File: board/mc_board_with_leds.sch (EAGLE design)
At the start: 30 parts, among them IC2 MEGA8-P, Q2 16MHz

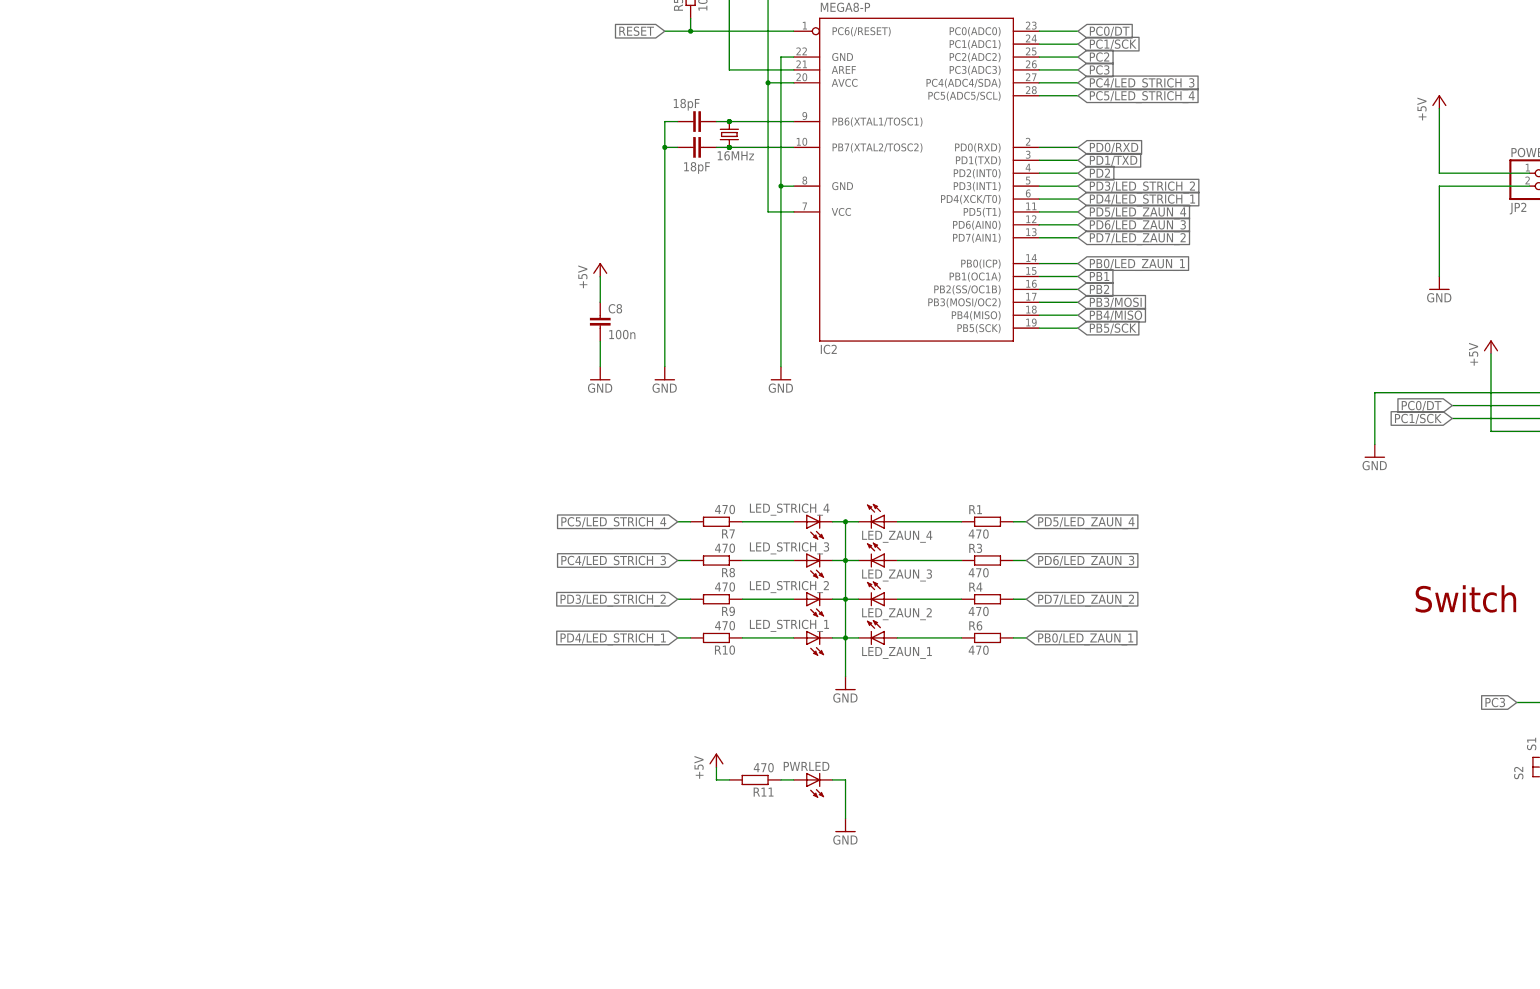
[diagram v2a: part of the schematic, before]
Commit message: added step up converter to schematic
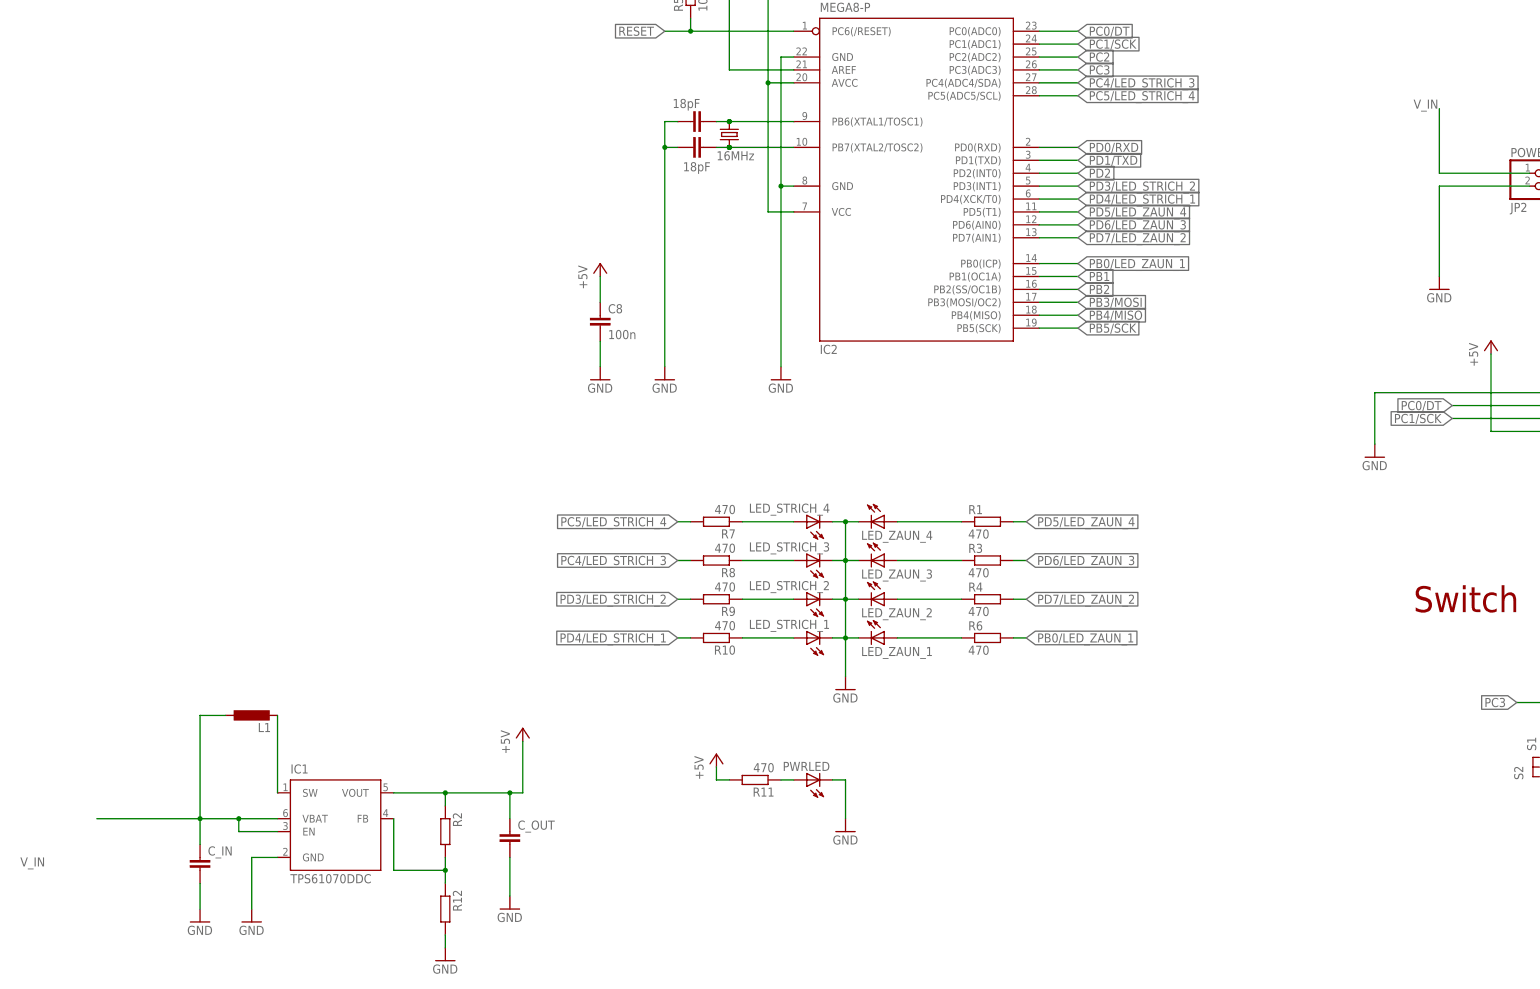
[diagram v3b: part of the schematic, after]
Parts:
- added C_IN, C_OUT: (no value), rcl-2:C-EUC0805
- added IC1: TPS61070DDC, texas:TPS61070DDC
- added L1: (no value), rcl:L-EUL4532P
- added R12, R2: (no value), resistor:R-EU_R0805
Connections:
- new net N$5: IC1.SW, L1.2
- new net N$6: IC1.FB, R12.1, R2.2
- new net V_IN: C_IN.1, IC1.EN, IC1.VBAT, L1.1, POWER1.1
- net +5V: now also C_OUT.1, IC1.VOUT, R2.1; no longer POWER1.1
- net GND: now also C_IN.2, C_OUT.2, IC1.GND, R12.2
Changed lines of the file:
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@@
 <part name="GND16" library="supply1" deviceset="GND" device=""/>
 <part name="POWER1" library="pinhead" deviceset="PINHD-1X2" device="" value="JP2"/>
-<part name="P+16" library="supply1" deviceset="+5V" device=""/>
 <part name="GND17" library="supply1" deviceset="GND" device=""/>
 <part name="HX1" library="pinhead" deviceset="PINHD-1X4" device="" value="JP1"/>
@@
 <part name="P+17" library="supply1" deviceset="+5V" device=""/>
 <part name="UART1" library="pinhead" deviceset="PINHD-1X2" device="" value="JP2"/>
+<part name="IC1" library="texas" deviceset="TPS6107*" device="DDC" technology="0"/>
+<part name="L1" library="rcl" deviceset="L-EU" device="L4532P"/>
+<part name="R2" library="resistor" deviceset="R-EU_" device="R0805"/>
+<part name="R12" library="resistor" deviceset="R-EU_" device="R0805"/>
+<part name="C_IN" library="rcl-2" deviceset="C-EU" device="C0805"/>
+<part name="C_OUT" library="rcl-2" deviceset="C-EU" device="C0805"/>
+<part name="GND1" library="supply1" deviceset="GND" device=""/>
+<part name="GND2" library="supply1" deviceset="GND" device=""/>
+<part name="P+1" library="supply1" deviceset="+5V" device=""/>
+<part name="GND3" library="supply1" deviceset="GND" device=""/>
+<part name="GND4" library="supply1" deviceset="GND" device=""/>
 </parts>
 <sheets>
@@
 <instance part="GND16" gate="1" x="327.66" y="109.22"/>
 <instance part="POWER1" gate="G$1" x="314.96" y="78.74"/>
-<instance part="P+16" gate="1" x="294.64" y="96.52"/>
 <instance part="GND17" gate="1" x="294.64" y="58.42"/>
 <instance part="HX1" gate="A" x="325.12" y="33.02"/>
@@
 <instance part="P+17" gate="1" x="304.8" y="48.26"/>
 <instance part="UART1" gate="G$1" x="353.06" y="60.96"/>
+<instance part="IC1" gate="G$1" x="76.2" y="-48.26"/>
+<instance part="L1" gate="G$1" x="60.96" y="-25.4" rot="R90"/>
+<instance part="R2" gate="G$1" x="99.06" y="-48.26" rot="R270"/>
+<instance part="R12" gate="G$1" x="99.06" y="-63.5" rot="R270"/>
+<instance part="C_IN" gate="G$1" x="50.8" y="-53.34"/>
+<instance part="C_OUT" gate="G$1" x="111.76" y="-48.26"/>
+<instance part="GND1" gate="1" x="50.8" y="-66.04"/>
+<instance part="GND2" gate="1" x="60.96" y="-66.04"/>
+<instance part="P+1" gate="1" x="114.3" y="-27.94"/>
+<instance part="GND3" gate="1" x="99.06" y="-73.66"/>
+<instance part="GND4" gate="1" x="111.76" y="-63.5"/>
 </instances>
 <busses>
@@
 <wire x1="281.94" y1="38.1" x2="281.94" y2="27.94" width="0.1524" layer="91"/>
 </segment>
+<segment>
+<pinref part="C_IN" gate="G$1" pin="2"/>
+<pinref part="GND1" gate="1" pin="GND"/>
+<wire x1="50.8" y1="-58.42" x2="50.8" y2="-63.5" width="0.1524" layer="91"/>
+</segment>
+<segment>
+<pinref part="GND2" gate="1" pin="GND"/>
+<pinref part="IC1" gate="G$1" pin="GND"/>
+<wire x1="60.96" y1="-63.5" x2="60.96" y2="-53.34" width="0.1524" layer="91"/>
+<wire x1="60.96" y1="-53.34" x2="66.04" y2="-53.34" width="0.1524" layer="91"/>
+</segment>
+<segment>
+<pinref part="GND4" gate="1" pin="GND"/>
+<pinref part="C_OUT" gate="G$1" pin="2"/>
+<wire x1="111.76" y1="-60.96" x2="111.76" y2="-53.34" width="0.1524" layer="91"/>
+</segment>
+<segment>
+<pinref part="GND3" gate="1" pin="GND"/>
+<pinref part="R12" gate="G$1" pin="2"/>
+<wire x1="99.06" y1="-71.12" x2="99.06" y2="-68.58" width="0.1524" layer="91"/>
+</segment>
 </net>
 <net name="N$8" class="0">
@@
 </segment>
 <segment>
-<pinref part="P+16" gate="1" pin="+5V"/>
-<wire x1="294.64" y1="93.98" x2="294.64" y2="81.28" width="0.1524" layer="91"/>
-<pinref part="POWER1" gate="G$1" pin="1"/>
-<wire x1="294.64" y1="81.28" x2="312.42" y2="81.28" width="0.1524" layer="91"/>
-</segment>
-<segment>
 <pinref part="HX1" gate="A" pin="4"/>
 <wire x1="322.58" y1="30.48" x2="304.8" y2="30.48" width="0.1524" layer="91"/>
 <pinref part="P+17" gate="1" pin="+5V"/>
 <wire x1="304.8" y1="30.48" x2="304.8" y2="45.72" width="0.1524" layer="91"/>
+</segment>
+<segment>
+<pinref part="IC1" gate="G$1" pin="VOUT"/>
+<wire x1="88.9" y1="-40.64" x2="99.06" y2="-40.64" width="0.1524" layer="91"/>
+<pinref part="R2" gate="G$1" pin="1"/>
+<wire x1="99.06" y1="-40.64" x2="111.76" y2="-40.64" width="0.1524" layer="91"/>
+<wire x1="111.76" y1="-40.64" x2="114.3" y2="-40.64" width="0.1524" layer="91"/>
+<wire x1="99.06" y1="-43.18" x2="99.06" y2="-40.64" width="0.1524" layer="91"/>
+<junction x="99.06" y="-40.64"/>
+<pinref part="P+1" gate="1" pin="+5V"/>
+<wire x1="114.3" y1="-40.64" x2="114.3" y2="-30.48" width="0.1524" layer="91"/>
+<pinref part="C_OUT" gate="G$1" pin="1"/>
+<wire x1="111.76" y1="-45.72" x2="111.76" y2="-40.64" width="0.1524" layer="91"/>
+<junction x="111.76" y="-40.64"/>
 </segment>
 </net>
@@
 </segment>
 </net>
+<net name="V_IN" class="0">
+<segment>
+<wire x1="294.64" y1="93.98" x2="294.64" y2="81.28" width="0.1524" layer="91"/>
+<pinref part="POWER1" gate="G$1" pin="1"/>
+<wire x1="294.64" y1="81.28" x2="312.42" y2="81.28" width="0.1524" layer="91"/>
+<label x="289.56" y="93.98" size="1.778" layer="95"/>
+</segment>
+<segment>
+<pinref part="IC1" gate="G$1" pin="VBAT"/>
+<wire x1="66.04" y1="-45.72" x2="58.42" y2="-45.72" width="0.1524" layer="91"/>
+<pinref part="C_IN" gate="G$1" pin="1"/>
+<wire x1="58.42" y1="-45.72" x2="50.8" y2="-45.72" width="0.1524" layer="91"/>
+<wire x1="50.8" y1="-45.72" x2="30.48" y2="-45.72" width="0.1524" layer="91"/>
+<wire x1="50.8" y1="-50.8" x2="50.8" y2="-45.72" width="0.1524" layer="91"/>
+<junction x="50.8" y="-45.72"/>
+<label x="20.32" y="-53.34" size="1.778" layer="95" rot="R180"/>
+<pinref part="L1" gate="G$1" pin="1"/>
+<wire x1="55.88" y1="-25.4" x2="50.8" y2="-25.4" width="0.1524" layer="91"/>
+<wire x1="50.8" y1="-25.4" x2="50.8" y2="-45.72" width="0.1524" layer="91"/>
+<pinref part="IC1" gate="G$1" pin="EN"/>
+<wire x1="66.04" y1="-48.26" x2="58.42" y2="-48.26" width="0.1524" layer="91"/>
+<wire x1="58.42" y1="-48.26" x2="58.42" y2="-45.72" width="0.1524" layer="91"/>
+<junction x="58.42" y="-45.72"/>
+</segment>
+</net>
+<net name="N$5" class="0">
+<segment>
+<pinref part="IC1" gate="G$1" pin="SW"/>
+<pinref part="L1" gate="G$1" pin="2"/>
+<wire x1="66.04" y1="-40.64" x2="66.04" y2="-25.4" width="0.1524" layer="91"/>
+</segment>
+</net>
+<net name="N$6" class="0">
+<segment>
+<pinref part="R12" gate="G$1" pin="1"/>
+<pinref part="R2" gate="G$1" pin="2"/>
+<wire x1="99.06" y1="-58.42" x2="99.06" y2="-55.88" width="0.1524" layer="91"/>
+<pinref part="IC1" gate="G$1" pin="FB"/>
+<wire x1="99.06" y1="-55.88" x2="99.06" y2="-53.34" width="0.1524" layer="91"/>
+<wire x1="88.9" y1="-45.72" x2="88.9" y2="-55.88" width="0.1524" layer="91"/>
+<wire x1="88.9" y1="-55.88" x2="99.06" y2="-55.88" width="0.1524" layer="91"/>
+<junction x="99.06" y="-55.88"/>
+</segment>
+</net>

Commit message: added missing values
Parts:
- C_IN: value (none) -> 4.7μF
- C_OUT: value (none) -> 47μF
- L1: value (none) -> 4,7µH
- R_BOT: value (none) -> 330k
- R_TOP: value (none) -> 560k
- renumbered IC1 to MCP1640BT-I, R12 to R_BOT, R2 to R_TOP
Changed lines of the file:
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@@
 <part name="P+17" library="supply1" deviceset="+5V" device=""/>
 <part name="UART1" library="pinhead" deviceset="PINHD-1X2" device="" value="JP2"/>
-<part name="IC1" library="texas" deviceset="TPS6107*" device="DDC" technology="0"/>
-<part name="L1" library="rcl" deviceset="L-EU" device="L4532P"/>
-<part name="R2" library="resistor" deviceset="R-EU_" device="R0805"/>
-<part name="R12" library="resistor" deviceset="R-EU_" device="R0805"/>
-<part name="C_IN" library="rcl-2" deviceset="C-EU" device="C0805"/>
-<part name="C_OUT" library="rcl-2" deviceset="C-EU" device="C0805"/>
+<part name="MCP1640BT-I" library="texas" deviceset="TPS6107*" device="DDC" technology="0"/>
+<part name="L1" library="rcl" deviceset="L-EU" device="L4532P" value="4,7µH"/>
+<part name="R_TOP" library="resistor" deviceset="R-EU_" device="R0805" value="560k"/>
+<part name="R_BOT" library="resistor" deviceset="R-EU_" device="R0805" value="330k"/>
+<part name="C_IN" library="rcl-2" deviceset="C-EU" device="C0805" value="4.7μF"/>
+<part name="C_OUT" library="rcl-2" deviceset="C-EU" device="C0805" value="47μF"/>
 <part name="GND1" library="supply1" deviceset="GND" device=""/>
 <part name="GND2" library="supply1" deviceset="GND" device=""/>
@@
 <instance part="P+17" gate="1" x="304.8" y="48.26"/>
 <instance part="UART1" gate="G$1" x="353.06" y="60.96"/>
-<instance part="IC1" gate="G$1" x="76.2" y="-48.26"/>
+<instance part="MCP1640BT-I" gate="G$1" x="76.2" y="-48.26"/>
 <instance part="L1" gate="G$1" x="60.96" y="-25.4" rot="R90"/>
-<instance part="R2" gate="G$1" x="99.06" y="-48.26" rot="R270"/>
-<instance part="R12" gate="G$1" x="99.06" y="-63.5" rot="R270"/>
+<instance part="R_TOP" gate="G$1" x="99.06" y="-48.26" rot="R270"/>
+<instance part="R_BOT" gate="G$1" x="99.06" y="-63.5" rot="R270"/>
 <instance part="C_IN" gate="G$1" x="50.8" y="-53.34"/>
 <instance part="C_OUT" gate="G$1" x="111.76" y="-48.26"/>
@@
 <segment>
 <pinref part="GND2" gate="1" pin="GND"/>
-<pinref part="IC1" gate="G$1" pin="GND"/>
+<pinref part="MCP1640BT-I" gate="G$1" pin="GND"/>
 <wire x1="60.96" y1="-63.5" x2="60.96" y2="-53.34" width="0.1524" layer="91"/>
 <wire x1="60.96" y1="-53.34" x2="66.04" y2="-53.34" width="0.1524" layer="91"/>
@@
 <segment>
 <pinref part="GND3" gate="1" pin="GND"/>
-<pinref part="R12" gate="G$1" pin="2"/>
+<pinref part="R_BOT" gate="G$1" pin="2"/>
 <wire x1="99.06" y1="-71.12" x2="99.06" y2="-68.58" width="0.1524" layer="91"/>
 </segment>
@@
 </segment>
 <segment>
-<pinref part="IC1" gate="G$1" pin="VOUT"/>
+<pinref part="MCP1640BT-I" gate="G$1" pin="VOUT"/>
 <wire x1="88.9" y1="-40.64" x2="99.06" y2="-40.64" width="0.1524" layer="91"/>
-<pinref part="R2" gate="G$1" pin="1"/>
+<pinref part="R_TOP" gate="G$1" pin="1"/>
 <wire x1="99.06" y1="-40.64" x2="111.76" y2="-40.64" width="0.1524" layer="91"/>
 <wire x1="111.76" y1="-40.64" x2="114.3" y2="-40.64" width="0.1524" layer="91"/>
@@
 </segment>
 <segment>
-<pinref part="IC1" gate="G$1" pin="VBAT"/>
+<pinref part="MCP1640BT-I" gate="G$1" pin="VBAT"/>
 <wire x1="66.04" y1="-45.72" x2="58.42" y2="-45.72" width="0.1524" layer="91"/>
 <pinref part="C_IN" gate="G$1" pin="1"/>
@@
 <wire x1="55.88" y1="-25.4" x2="50.8" y2="-25.4" width="0.1524" layer="91"/>
 <wire x1="50.8" y1="-25.4" x2="50.8" y2="-45.72" width="0.1524" layer="91"/>
-<pinref part="IC1" gate="G$1" pin="EN"/>
+<pinref part="MCP1640BT-I" gate="G$1" pin="EN"/>
 <wire x1="66.04" y1="-48.26" x2="58.42" y2="-48.26" width="0.1524" layer="91"/>
 <wire x1="58.42" y1="-48.26" x2="58.42" y2="-45.72" width="0.1524" layer="91"/>
@@
 <net name="N$5" class="0">
 <segment>
-<pinref part="IC1" gate="G$1" pin="SW"/>
+<pinref part="MCP1640BT-I" gate="G$1" pin="SW"/>
 <pinref part="L1" gate="G$1" pin="2"/>
 <wire x1="66.04" y1="-40.64" x2="66.04" y2="-25.4" width="0.1524" layer="91"/>
@@
 <net name="N$6" class="0">
 <segment>
-<pinref part="R12" gate="G$1" pin="1"/>
-<pinref part="R2" gate="G$1" pin="2"/>
+<pinref part="R_BOT" gate="G$1" pin="1"/>
+<pinref part="R_TOP" gate="G$1" pin="2"/>
 <wire x1="99.06" y1="-58.42" x2="99.06" y2="-55.88" width="0.1524" layer="91"/>
-<pinref part="IC1" gate="G$1" pin="FB"/>
+<pinref part="MCP1640BT-I" gate="G$1" pin="FB"/>
 <wire x1="99.06" y1="-55.88" x2="99.06" y2="-53.34" width="0.1524" layer="91"/>
 <wire x1="88.9" y1="-45.72" x2="88.9" y2="-55.88" width="0.1524" layer="91"/>
